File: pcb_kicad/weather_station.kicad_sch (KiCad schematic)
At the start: 0 parts

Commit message: Added initial circuit diagram
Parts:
- added BT1: Battery_Cell, symbol Device:Battery_Cell
- added C1, C4: 22u, symbol Device:C
- added C2: 10u, symbol Device:C
- added C3: 100n, symbol Device:C
- added D1: LED, symbol Device:LED
- added J1: USB_B_Micro, symbol Connector:USB_B_Micro
- added J2: Conn_02x05_Odd_Even, Connector_IDC:IDC-Header_2x05_P2.54mm_Vertical, symbol Connector_Generic:Conn_02x05_Odd_Even
- added J3: Conn_02x03_Odd_Even, Connector_IDC:IDC-Header_2x03_P2.54mm_Vertical, symbol Connector_Generic:Conn_02x03_Odd_Even
- added R1: 1000, symbol Device:R
- added R2: 500, symbol Device:R
- added U1: ESP32-S3, Package_DFN_QFN:QFN-56-1EP_7x7mm_P0.4mm_EP4x4mm, symbol MCU_Espressif:ESP32-S3
- added U2: BMP280, Package_LGA:Bosch_LGA-8_2.5x2.5mm_P0.65mm_ClockwisePinNumbering, symbol Sensor_Pressure:BMP280
- added U3: AM2302, Sensor:ASAIR_AM2302_P2.54mm_Vertical, symbol Sensor:AM2302
- added U4: ADP5063, Package_DFN_QFN:QFN-20-1EP_4x4mm_P0.5mm_EP2.5x2.5mm, symbol Battery_Management:ADP5063
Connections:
- new net: U1.10 (GPIO5), U3.1 (VDD)
- new net: U1.2 (VDD3P3), U1.3 (VDD3P3)
- new net: C4.1, U1.20 (VDD3P3_RTC), U4.10 (ISO_Sx), U4.11 (ISO_Sx), U4.9 (ISO_Sx)
- new net: J2.1 (Pin_1), J3.2 (Pin_2), U1.27 (GPIO21)
- new net: J3.1 (Pin_1), U1.4 (CHIP_PU)
- new net: R2.2, U1.43 (GPIO38)
- new net: J2.4 (Pin_4), U1.44 (MTCK)
- new net: J2.6 (Pin_6), U1.45 (MTDO)
- new net: J2.8 (Pin_8), U1.47 (MTDI)
- new net: J2.2 (Pin_2), U1.48 (MTMS)
- new net: J3.3 (Pin_3), U1.49 (U0TXD)
- new net: J3.6 (Pin_6), U1.5 (GPIO0)
- new net: J3.5 (Pin_5), U1.50 (U0RXD)
- new net: R1.2, U1.55 (VDDA), U1.56 (VDDA)
- new net: U1.7 (GPIO2), U2.4 (SCK)
- new net: U1.8 (GPIO3), U2.3 (SDI)
- new net: U1.9 (GPIO4), U3.2 (SDA)
- new net: D1.1 (K), U4.15 (ILED)
- new net: D1.2 (A), R2.1
- new net: BT1.1 (+), C1.1, U4.12 (ISO_Bx), U4.13 (ISO_Bx), U4.14 (ISO_Bx), U4.4 (BAT_SNS)
- new net: C3.1, U4.19 (CBP)
- new net: C2.1, J1.1 (VBUS), U4.2 (D_IO3), U4.5 (D_IO1), U4.6 (VINx), U4.7 (VINx), U4.8 (VINx)
- new net: U2.2 (CSB), U2.6 (VDDIO)
- new net: R1.1, U2.8 (VDD)
- new net Earth: C2.2, C3.2, J1.5 (GND), J1.6 (Shield), U4.3 (D_IO2)
- new net GND: BT1.2 (-), C1.2, C4.2, J2.3 (Pin_3), J2.5 (Pin_5), J2.7 (Pin_7), J2.9 (Pin_9), J3.4 (Pin_4), U1.57 (GND), U2.1 (GND), U2.5 (SDO), U2.7 (GND), U3.3 (GND), U3.4 (GND), U4.18 (THR), U4.20 (GND)

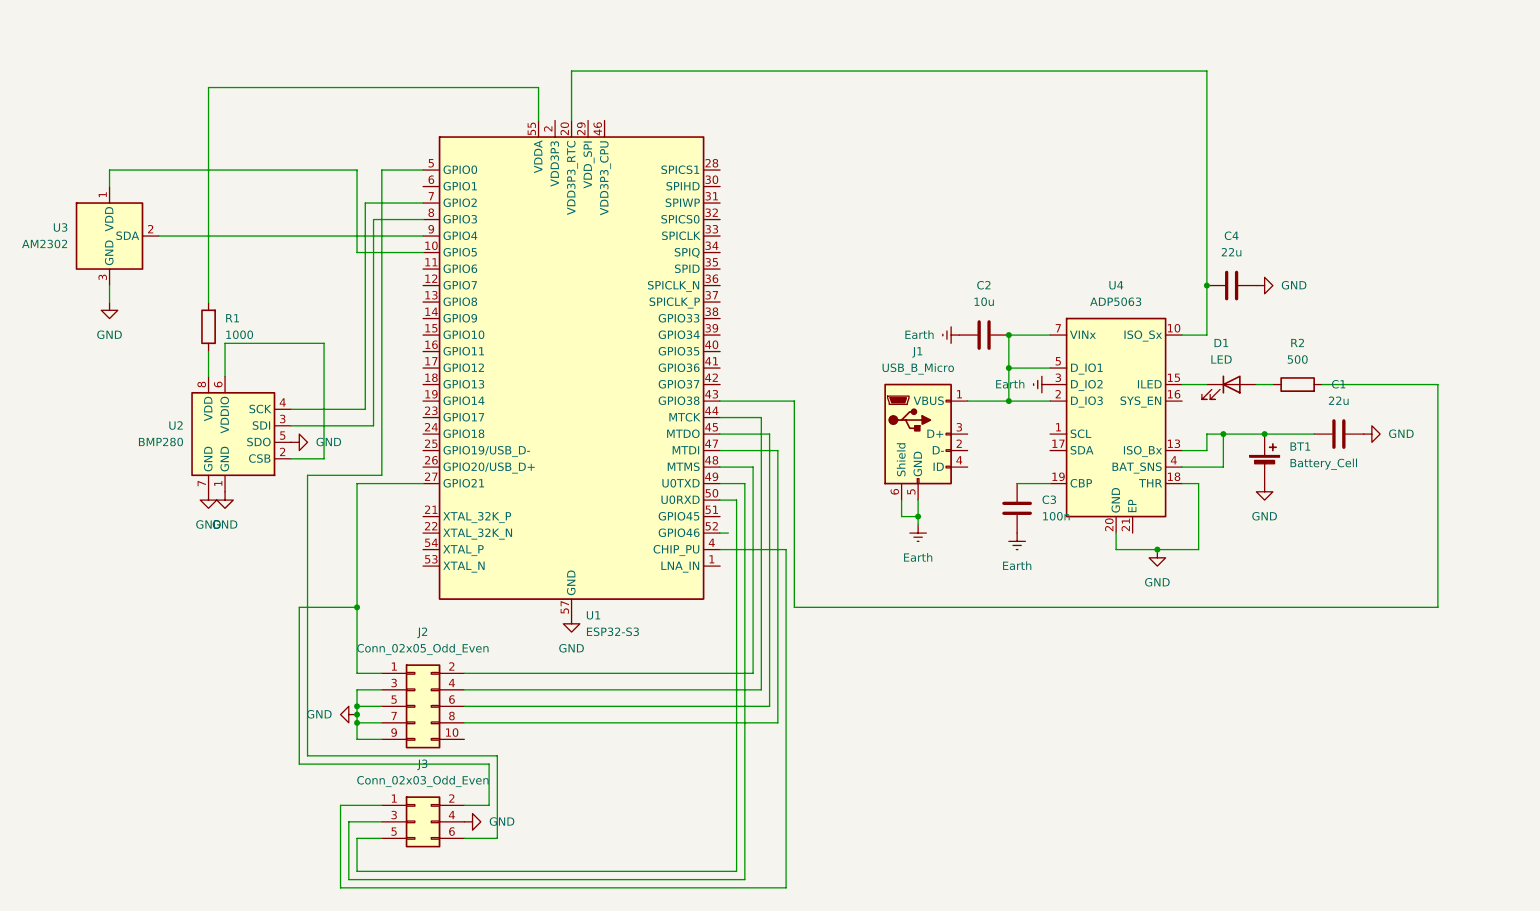
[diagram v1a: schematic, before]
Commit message: changed esp32 soc to the esp32wroom
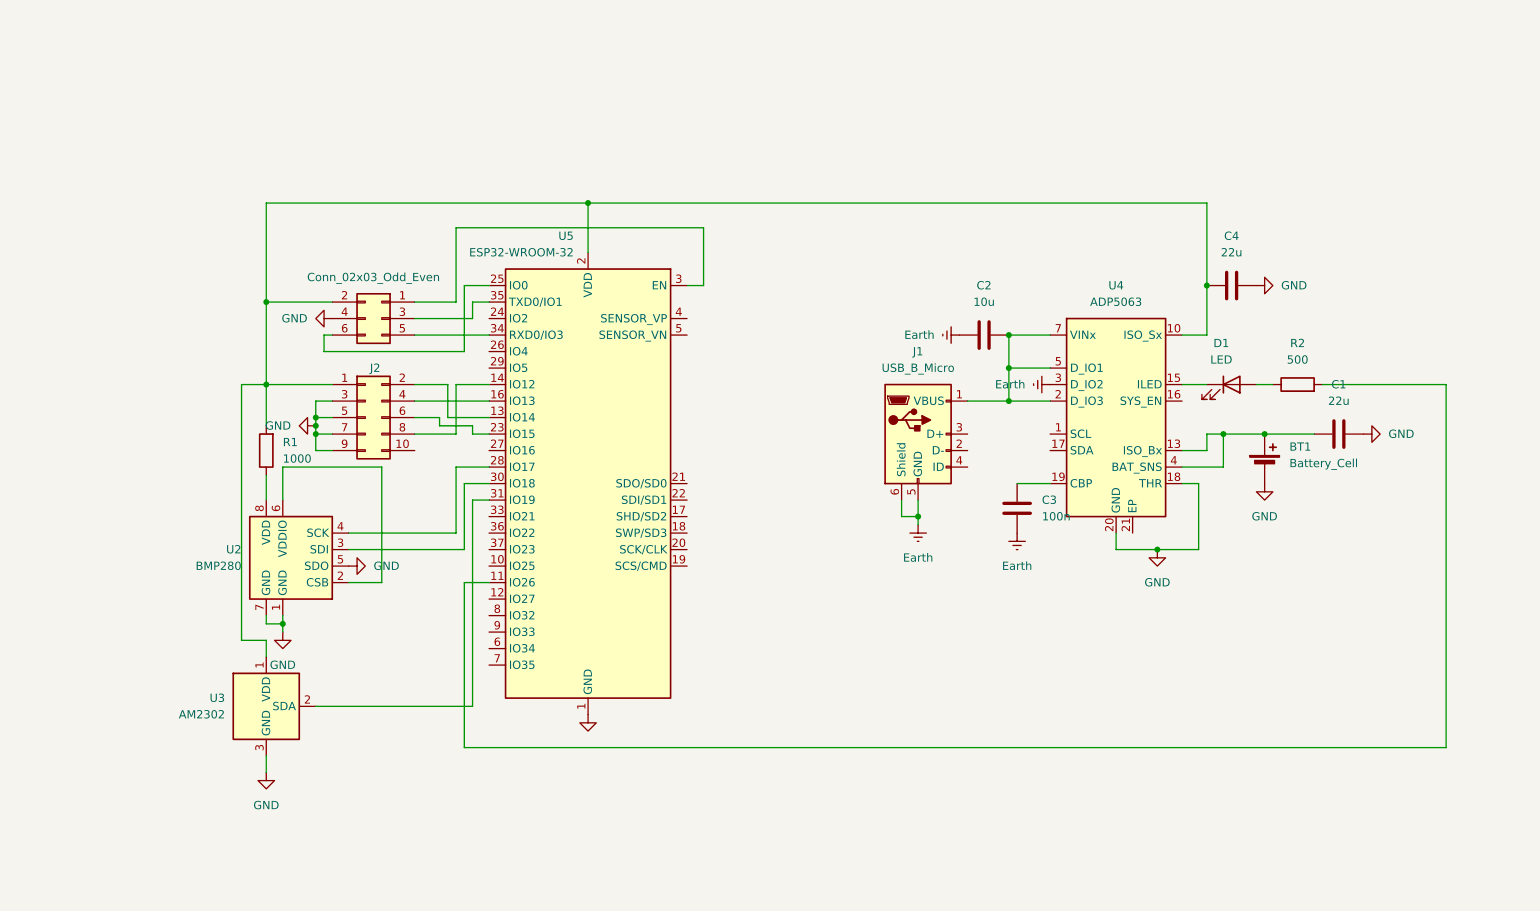
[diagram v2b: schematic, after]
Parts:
- removed U1: ESP32-S3, Package_DFN_QFN:QFN-56-1EP_7x7mm_P0.4mm_EP4x4mm, symbol MCU_Espressif:ESP32-S3
- added U5: ESP32-WROOM-32, RF_Module:ESP32-WROOM-32E, symbol RF_Module:ESP32-WROOM-32
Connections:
- net GND: now also U5.1 (GND), U5.15 (GND), U5.38 (GND), U5.39 (GND)
- net at U3.1 (VDD): now also C4.1, J2.1 (Pin_1), J3.2 (Pin_2), R1.2, U4.10 (ISO_Sx), U4.11 (ISO_Sx), U4.9 (ISO_Sx), U5.2 (VDD)
- net at J3.1 (Pin_1): now also U5.3 (EN)
- net at R2.2: now also U5.11 (IO26)
- net at J2.4 (Pin_4): now also U5.16 (IO13)
- net at J2.6 (Pin_6): now also U5.23 (IO15)
- net at J2.8 (Pin_8): now also U5.14 (IO12)
- net at J2.2 (Pin_2): now also U5.13 (IO14)
- net at J3.3 (Pin_3): now also U5.35 (TXD0/IO1)
- net at J3.6 (Pin_6): now also U5.25 (IO0)
- net at J3.5 (Pin_5): now also U5.34 (RXD0/IO3)
- net at U2.4 (SCK): now also U5.28 (IO17)
- net at U2.3 (SDI): now also U5.30 (IO18)
- net at U3.2 (SDA): now also U5.31 (IO19)
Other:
- moved on the sheet: J2, R1, U2, U3

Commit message: added voltage regulator circuit for BMP280 VDDIO and and an alternative connection point for BMP280 module
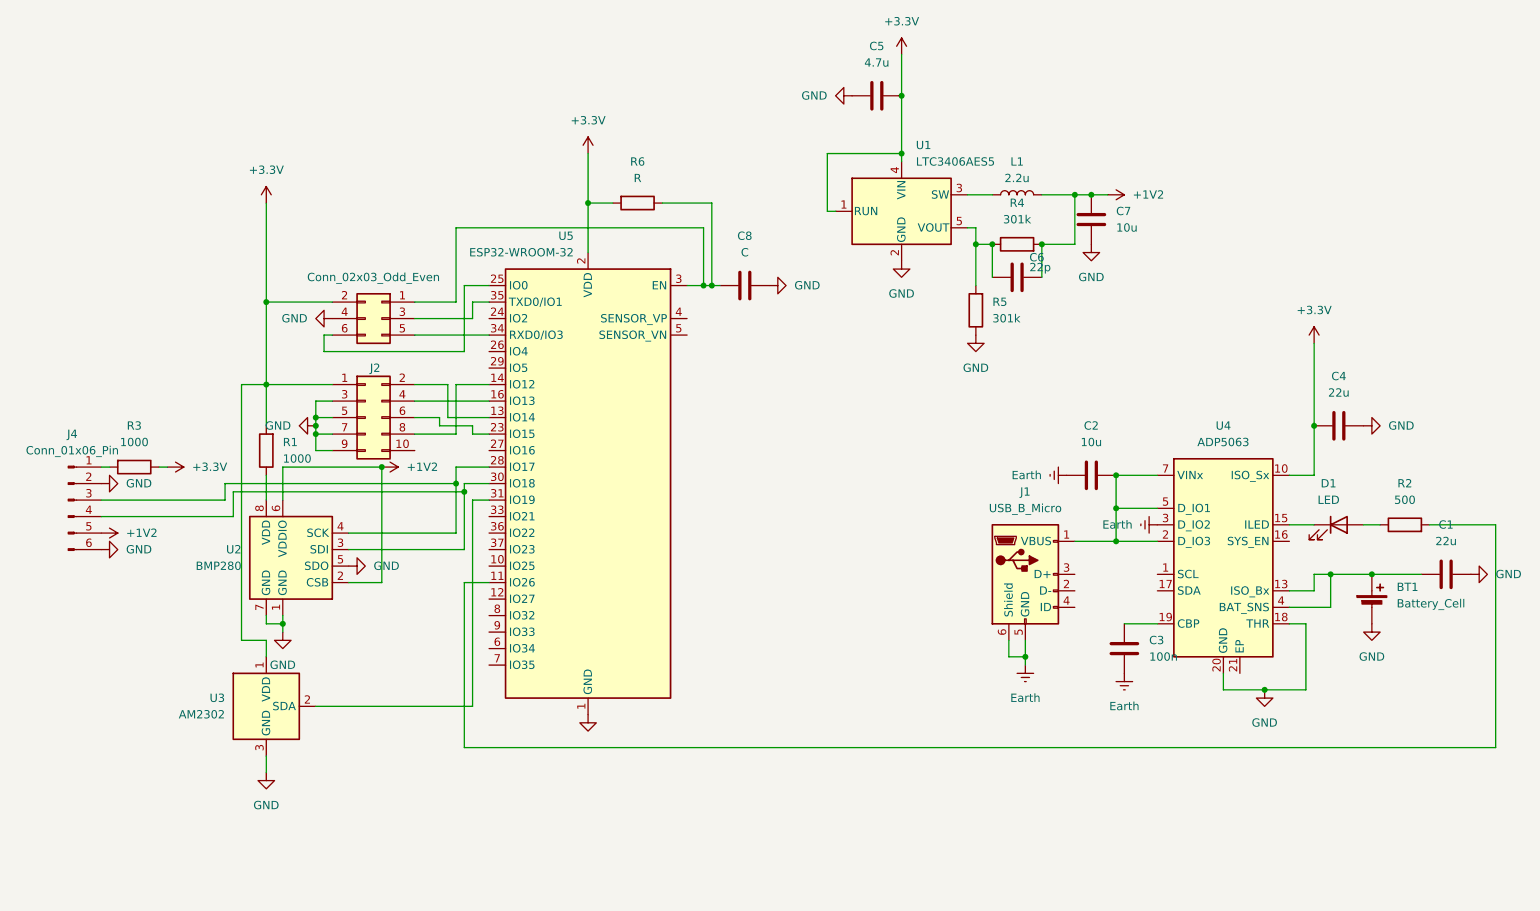
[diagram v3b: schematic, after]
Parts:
- added C5: 4.7u, symbol Device:C
- added C6: 22p, symbol Device:C
- added C7: 10u, symbol Device:C
- added C8: C, symbol Device:C
- added J4: Conn_01x06_Pin, Connector_PinHeader_2.54mm:PinHeader_1x06_P2.54mm_Vertical, symbol Connector:Conn_01x06_Pin
- added L1: 2.2u, symbol Device:L
- added R3: 1000, symbol Device:R
- added R4, R5: 301k, symbol Device:R
- added R6: R, symbol Device:R
- added U1: LTC3406AES5, Package_TO_SOT_SMD:TSOT-23-5, symbol Regulator_Switching:LTC3406AES5
- U5: footprint RF_Module:ESP32-WROOM-32E -> RF_Module:ESP32-WROOM-32D; symbol RF_Module:ESP32-WROOM-32 -> RF_Module:ESP32-WROOM-32E
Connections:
- net GND: now also C5.1, C7.1, C8.2, J4.2 (Pin_2), J4.6 (Pin_6), R5.1, U1.2 (GND)
- net +3.3V: now reaches C4.1, J2.1 (Pin_1), J3.2 (Pin_2), R1.2, U3.1 (VDD), U4.10 (ISO_Sx), U4.11 (ISO_Sx), U4.9 (ISO_Sx), U5.2 (VDD)
- net +3.3V: now also C5.2, R3.1, R6.2, U1.1 (RUN), U1.4 (VIN)
- net +1V2: now reaches U2.2 (CSB), U2.6 (VDDIO)
- net +1V2: now also C6.2, C7.2, J4.5 (Pin_5), L1.2, R4.2
- net at U2.3 (SDI), U5.30 (IO18): now also J4.4 (Pin_4)
- net at U2.4 (SCK), U5.28 (IO17): now also J4.3 (Pin_3)
- net at J3.1 (Pin_1), U5.3 (EN): now also C8.1, R6.1
- new net: L1.1, U1.3 (SW)
- new net: C6.1, R4.1, R5.2, U1.5 (VOUT)
- new net: J4.1 (Pin_1), R3.2
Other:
- moved on the sheet: BT1, C1, C2, C3, C4, D1, J1, R2, U4

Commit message: added full pcb schematic
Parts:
- removed C6: 22p, symbol Device:C
- removed L1: 2.2u, symbol Device:L
- removed U1: LTC3406AES5, Package_TO_SOT_SMD:TSOT-23-5, symbol Regulator_Switching:LTC3406AES5
- added C10, C9: 100n, Capacitor_SMD:C_0603_1608Metric_Pad1.08x0.95mm_HandSolder, symbol Device:C
- added J5: Conn_01x02_Pin, TestPoint:TestPoint_2Pads_Pitch2.54mm_Drill0.8mm, symbol Connector:Conn_01x02_Pin
- added R7: 0R, Resistor_SMD:R_0603_1608Metric_Pad0.98x0.95mm_HandSolder, symbol Device:R
- added R8, R9: 5.1k, Resistor_SMD:R_0603_1608Metric_Pad0.98x0.95mm_HandSolder, symbol Device:R
- added U6: LD1117S33TR_SOT223, Package_TO_SOT_SMD:SOT-223-3_TabPin2, symbol Regulator_Linear:LD1117S33TR_SOT223
- BT1: footprint (none) -> Battery:BatteryHolder_Keystone_1042_1x18650
- C1, C2, C3, C4, C7: footprint (none) -> Capacitor_SMD:C_0603_1608Metric_Pad1.08x0.95mm_HandSolder
- C5: value 4.7u -> 100nf; footprint (none) -> Capacitor_SMD:C_0603_1608Metric_Pad1.08x0.95mm_HandSolder
- C8: value C -> 0.1uF; footprint (none) -> Capacitor_SMD:C_0603_1608Metric_Pad1.08x0.95mm_HandSolder
- D1: footprint (none) -> LED_SMD:LED_0603_1608Metric_Pad1.05x0.95mm_HandSolder
- J1: value USB_B_Micro -> USB_C_Receptacle_PowerOnly_6P; footprint (none) -> Connector_USB:USB_C_Receptacle_GCT_USB4125-xx-x-0190_6P_TopMnt_Horizontal; symbol Connector:USB_B_Micro -> Connector:USB_C_Receptacle_PowerOnly_6P
- R1, R2, R3: footprint (none) -> Resistor_SMD:R_0603_1608Metric_Pad0.98x0.95mm_HandSolder
- R4, R5: value 301k -> 0R; footprint (none) -> Resistor_SMD:R_0603_1608Metric_Pad0.98x0.95mm_HandSolder
- R6: value R -> 10k; footprint (none) -> Resistor_SMD:R_0603_1608Metric_Pad0.98x0.95mm_HandSolder
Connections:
- net +3.3V: now also C7.2, J4.5 (Pin_5), R2.2, U2.2 (CSB), U2.6 (VDDIO), C9.1, U6.2 (VO); no longer C5.2
- net Earth: now also J1.A12 (GND), J1.B12 (GND), J1.S1 (SHIELD), R5.2, R8.1, R9.2; no longer J1.5 (GND), J1.6 (Shield)
- net GND: now also C5.2, U4.1 (SCL), U4.16 (SYS_EN), U4.17 (SDA), C10.2, C9.2, U6.1 (GND); no longer C5.1
- net at C2.1, U4.2 (D_IO3), U4.5 (D_IO1)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: now also R7.2; no longer J1.1 (VBUS)
- net at R1.1, U2.8 (VDD): now also C10.1
- net at R4.1: now also J1.A9 (VBUS), J1.B9 (VBUS), R7.1; no longer R5.2
- net at U5.11 (IO26): no longer R2.2
- net at U5.26 (IO4): now also J5.1 (Pin_1)
- net at U5.29 (IO5): now also J5.2 (Pin_2)
- removed net +1V2: C7.2, J4.5 (Pin_5), R4.2, U2.2 (CSB), U2.6 (VDDIO)
- new net: J1.A5 (CC1), R9.1
- new net: J1.B5 (CC2), R8.2
- new net +5V: C5.1, R4.2, U6.3 (VI)
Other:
- moved on the sheet: C7

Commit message: added 0 ohm resistors for battery only mode, out pins for all unused pins from esp 32, opened blind vias and removed unsupported vias and silkscreen drawings from esp32 blueprint
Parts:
- added J6: Conn_01x11_Pin, Connector_PinHeader_2.54mm:PinHeader_1x11_P2.54mm_Vertical, symbol Connector:Conn_01x11_Pin
- added J7: Conn_01x01_Pin, Connector_PinSocket_2.54mm:PinSocket_1x01_P2.54mm_Vertical, symbol Connector:Conn_01x01_Pin
- added R10, R11: 0R, Resistor_SMD:R_0603_1608Metric_Pad0.98x0.95mm_HandSolder, symbol Device:R
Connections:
- net +3.3V: now also R10.2
- net at C1.1, U4.12 (ISO_Bx), U4.13 (ISO_Bx)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: now also R11.1; no longer BT1.1 (+)
- net at U5.10 (IO25): now also J6.5 (Pin_5)
- net at U5.11 (IO26): now also J6.6 (Pin_6)
- net at U5.12 (IO27): now also J6.7 (Pin_7)
- net at U5.24 (IO2): now also J7.1 (Pin_1)
- net at U5.27 (IO16): now also J6.1 (Pin_1)
- net at U5.33 (IO21): now also J6.2 (Pin_2)
- net at U5.36 (IO22): now also J6.3 (Pin_3)
- net at U5.37 (IO23): now also J6.4 (Pin_4)
- net at U5.6 (IO34): now also J6.10 (Pin_10)
- net at U5.7 (IO35): now also J6.11 (Pin_11)
- net at U5.8 (IO32): now also J6.8 (Pin_8)
- net at U5.9 (IO33): now also J6.9 (Pin_9)
- new net: BT1.1 (+), R10.1, R11.2
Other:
- moved on the sheet: BT1
